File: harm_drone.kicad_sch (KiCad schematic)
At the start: 0 parts

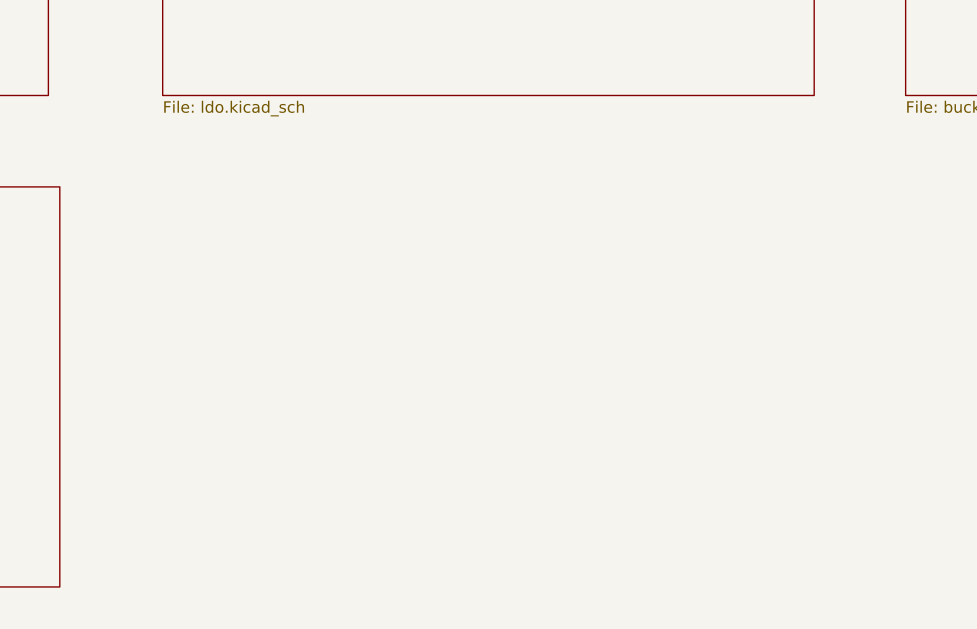
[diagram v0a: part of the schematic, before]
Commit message: USB-Serial Sheet Add
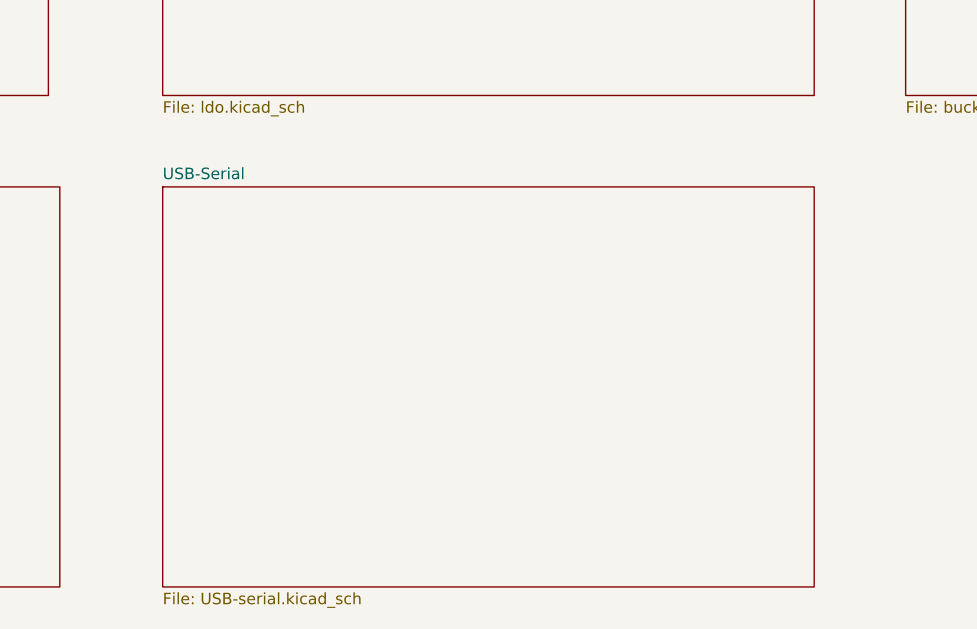
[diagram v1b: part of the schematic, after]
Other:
- added sheet USB-Serial (USB-serial.kicad_sch)
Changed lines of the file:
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@@
+	)
+	(sheet
+		(at 104.14 74.93)
+		(size 72.39 44.45)
+		(fields_autoplaced yes)
+		(stroke
+			(width 0.1524)
+			(type solid)
+		)
+		(fill
+			(color 0 0 0 0.0000)
+		)
+		(property "Sheetname" "USB-Serial"
+			(at 104.14 74.2184 0)
+			(effects
+				(font
+					(size 1.27 1.27)
+				)
+				(justify left bottom)
+			)
+		)
+		(property "Sheetfile" "USB-serial.kicad_sch"
+			(at 104.14 119.9646 0)
+			(effects
+				(font
+					(size 1.27 1.27)
+				)
+				(justify left top)
+			)
+		)
+		(instances
+			(project "harm_drone"
+				(path "/5ce3566e-4e0f-420e-9b0d-3952cd3c63fd"
+					(page "6")
+				)
+			)
+		)
 	)
 	(sheet

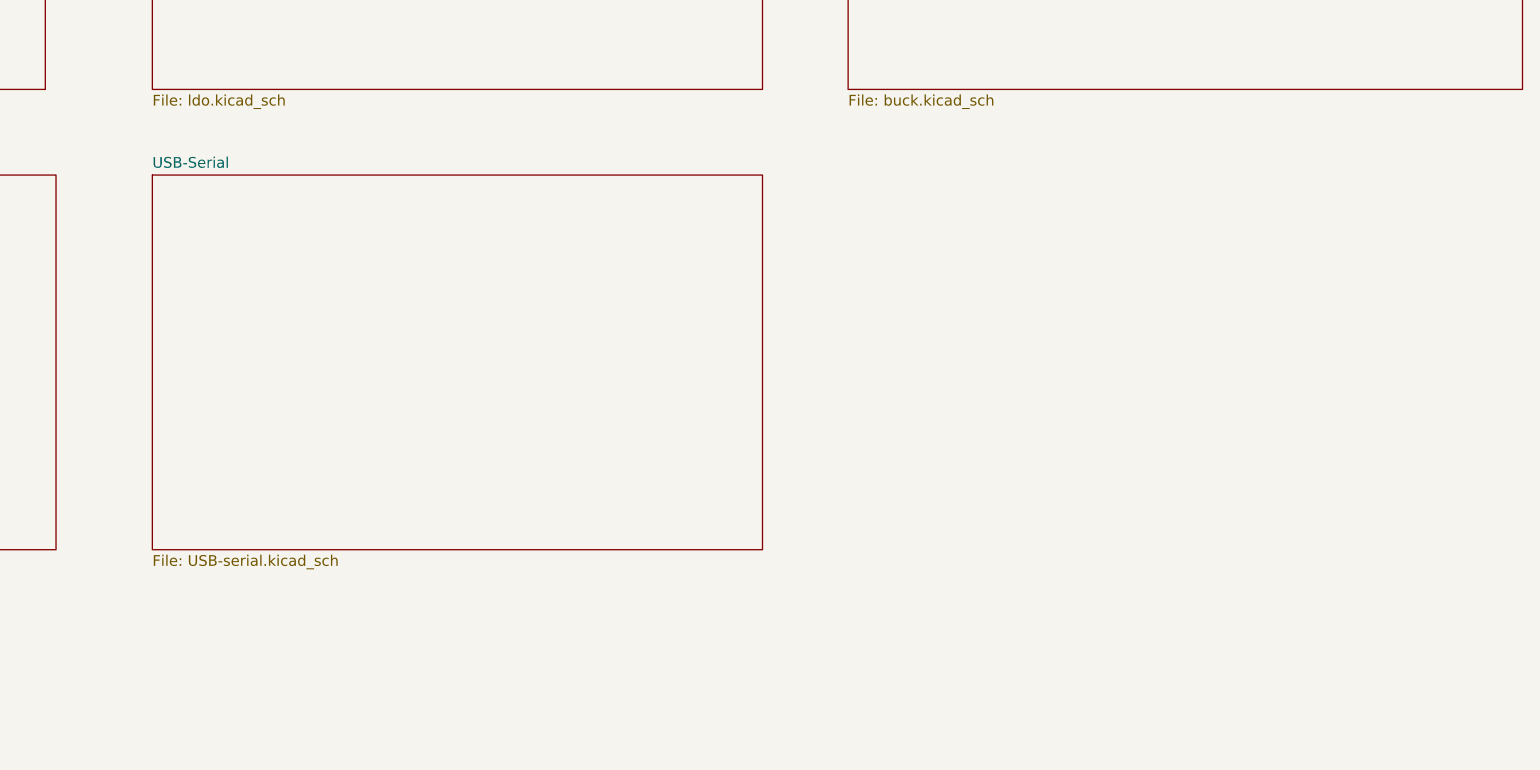
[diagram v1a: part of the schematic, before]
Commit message: Put grounds on SPI
Changed ground net to symbols
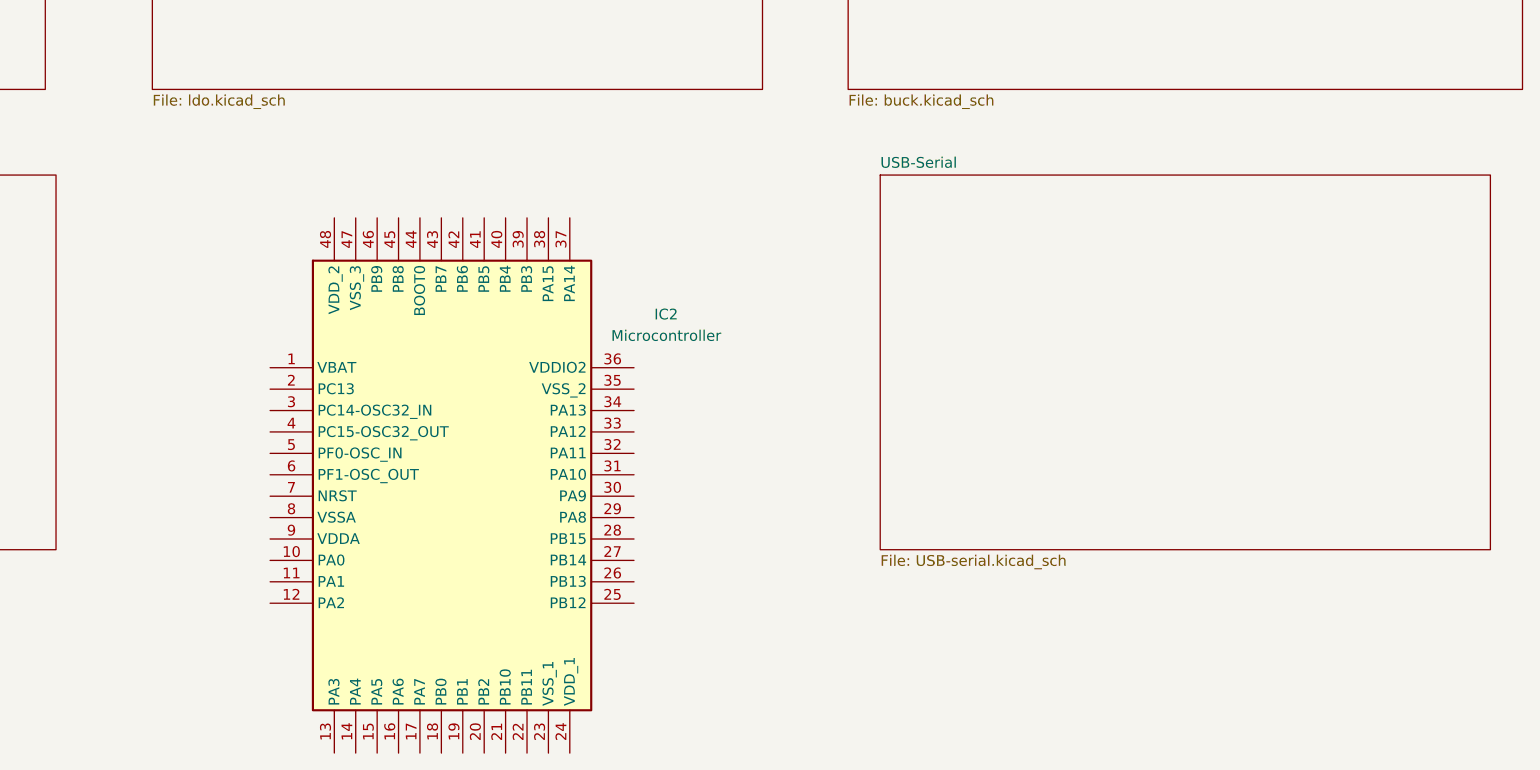
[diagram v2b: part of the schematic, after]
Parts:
- added IC2: Microcontroller, QFP50P900X900X160-48N, symbol group127:Microcontroller
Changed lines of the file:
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@@
 	(generator_version "8.0")
 	(paper "A4")
+	(symbol
+		(lib_id "group127:Microcontroller")
+		(at 118.11 97.79 0)
+		(unit 1)
+		(exclude_from_sim no)
+		(in_bom yes)
+		(on_board yes)
+		(dnp no)
+		(fields_autoplaced yes)
+		(property "Reference" "IC2"
+			(at 165.1 91.4714 0)
+			(effects
+				(font
+					(size 1.27 1.27)
+				)
+			)
+		)
+		(property "Value" "Microcontroller"
+			(at 165.1 94.0114 0)
+			(effects
+				(font
+					(size 1.27 1.27)
+				)
+			)
+		)
+		(property "Footprint" "QFP50P900X900X160-48N"
+			(at 157.48 182.55 0)
+			(effects
+				(font
+					(size 1.27 1.27)
+				)
+				(justify left top)
+				(hide yes)
+			)
+		)
+		(property "Datasheet" ""
+			(at 157.48 282.55 0)
+			(effects
+				(font
+					(size 1.27 1.27)
+				)
+				(justify left top)
+				(hide yes)
+			)
+		)
+		(property "Description" "STMICROELECTRONICS - STM32F072CBT6 - MCU, 32BIT, CORTEX-M0, 48MHZ, LQFP-48"
+			(at 118.11 97.79 0)
+			(effects
+				(font
+					(size 1.27 1.27)
+				)
+				(hide yes)
+			)
+		)
+		(property "Height" "1.6"
+			(at 157.48 482.55 0)
+			(effects
+				(font
+					(size 1.27 1.27)
+				)
+				(justify left top)
+				(hide yes)
+			)
+		)
+		(property "Mouser Part Number" "511-STM32F072CBT6"
+			(at 157.48 582.55 0)
+			(effects
+				(font
+					(size 1.27 1.27)
+				)
+				(justify left top)
+				(hide yes)
+			)
+		)
+		(property "Mouser Price/Stock" "https://www.mouser.co.uk/ProductDetail/STMicroelectronics/STM32F072CBT6?qs=xf9JV0PLFEfBqXx8wKtR8A%3D%3D"
+			(at 157.48 682.55 0)
+			(effects
+				(font
+					(size 1.27 1.27)
+				)
+				(justify left top)
+				(hide yes)
+			)
+		)
+		(property "Manufacturer_Name" "STMicroelectronics"
+			(at 157.48 782.55 0)
+			(effects
+				(font
+					(size 1.27 1.27)
+				)
+				(justify left top)
+				(hide yes)
+			)
+		)
+		(property "Manufacturer_Part_Number" "STM32F072CBT6"
+			(at 157.48 882.55 0)
+			(effects
+				(font
+					(size 1.27 1.27)
+				)
+				(justify left top)
+				(hide yes)
+			)
+		)
+		(pin "32"
+		)
+		(pin "30"
+		)
+		(pin "6"
+		)
+		(pin "7"
+		)
+		(pin "17"
+		)
+		(pin "28"
+		)
+		(pin "23"
+		)
+		(pin "15"
+		)
+		(pin "29"
+		)
+		(pin "37"
+		)
+		(pin "18"
+		)
+		(pin "34"
+		)
+		(pin "46"
+		)
+		(pin "48"
+		)
+		(pin "33"
+		)
+		(pin "39"
+		)
+		(pin "36"
+		)
+		(pin "4"
+		)
+		(pin "12"
+		)
+		(pin "35"
+		)
+		(pin "27"
+		)
+		(pin "42"
+		)
+		(pin "24"
+		)
+		(pin "5"
+		)
+		(pin "11"
+		)
+		(pin "16"
+		)
+		(pin "2"
+		)
+		(pin "22"
+		)
+		(pin "26"
+		)
+		(pin "45"
+		)
+		(pin "21"
+		)
+		(pin "43"
+		)
+		(pin "44"
+		)
+		(pin "47"
+		)
+		(pin "8"
+		)
+		(pin "13"
+		)
+		(pin "19"
+		)
+		(pin "20"
+		)
+		(pin "9"
+		)
+		(pin "10"
+		)
+		(pin "1"
+		)
+		(pin "3"
+		)
+		(pin "14"
+		)
+		(pin "40"
+		)
+		(pin "41"
+		)
+		(pin "25"
+		)
+		(pin "38"
+		)
+		(pin "31"
+		)
+		(instances
+			(project ""
+				(path "/5ce3566e-4e0f-420e-9b0d-3952cd3c63fd"
+					(reference "IC2")
+					(unit 1)
+				)
+			)
+		)
+	)
 	(sheet
 		(at 104.14 20.32)
@@
 	)
 	(sheet
-		(at 104.14 74.93)
+		(at 190.5 74.93)
 		(size 72.39 44.45)
 		(fields_autoplaced yes)
@@
 		)
 		(property "Sheetname" "USB-Serial"
-			(at 104.14 74.2184 0)
+			(at 190.5 74.2184 0)
 			(effects
 				(font
@@
 		)
 		(property "Sheetfile" "USB-serial.kicad_sch"
-			(at 104.14 119.9646 0)
-			(effects
-				(font
+			(at 190.5 119.9646 0)
+			(effects
+				(font

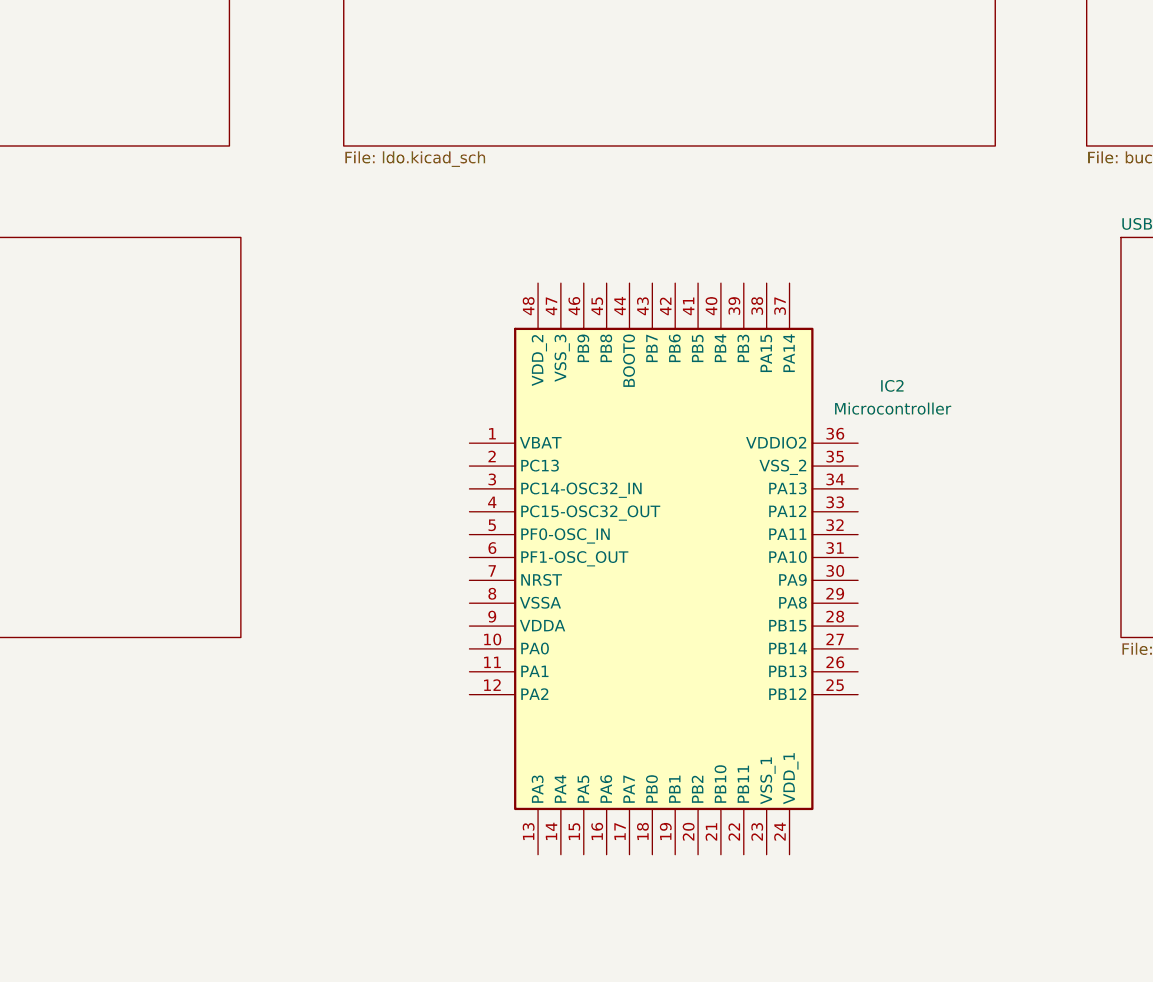
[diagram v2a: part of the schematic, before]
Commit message: Power and ground added on microcontroller
Added power and ground to microcontroller
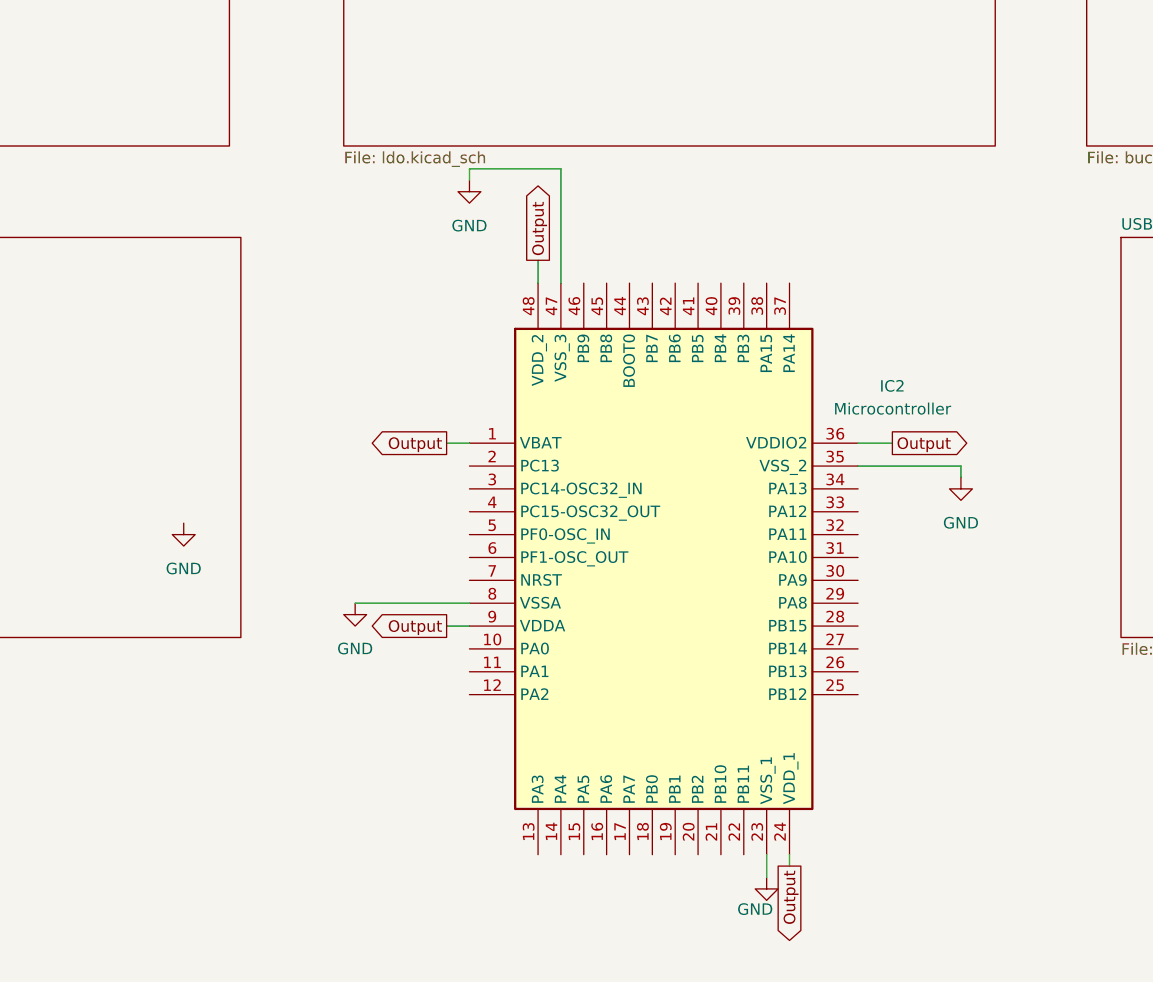
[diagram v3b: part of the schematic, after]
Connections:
- net Output: now reaches IC2.1 (VBAT)
- net Output: now also IC2.24 (VDD_1), IC2.36 (VDDIO2), IC2.48 (VDD_2), IC2.9 (VDDA)
- net GND: now reaches IC2.23 (VSS_1)
- net GND: now also IC2.35 (VSS_2), IC2.47 (VSS_3), IC2.8 (VSSA)
